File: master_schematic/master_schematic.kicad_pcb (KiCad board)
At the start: 4 copper layers, 157.5 x 111.9 mm, 82 parts, among them J1 Conn_01x02_Shielded, J10 0430450400, J11 1723103102, J12 1723103102, J13 1723103102, J14 1723103102, J15 1723103102, J16 1723103102, J17 1723103102, J18 1723103102, J19 1723103102, J2 0430450400, J20 1723103102, J3 0430450400, J4 0430450400, J5 0430450400, J6 0430450400, J7 0430450400, J8 0430450400, J9 0430450400, Q1 CWDM3011N TR13 PBFREE, Q10 CWDM3011N TR13 PBFREE, Q2 CWDM3011N TR13 PBFREE, Q3 CWDM3011N TR13 PBFREE, Q4 CWDM3011N TR13 PBFREE, Q5 CWDM3011N TR13 PBFREE, Q6 CWDM3011N TR13 PBFREE, Q7 CWDM3011N TR13 PBFREE, Q8 CWDM3011N TR13 PBFREE, Q9 CWDM3011N TR13 PBFREE, U1 RFM95, U10 HX711, U11 HX711, U2 teensy_4.1, U4 MCP9600_Module, U5 MCP9600_Module, U6 MCP9600_Module, U7 MCP9600_Module, U8 MCP9600_Module, U9 HX711

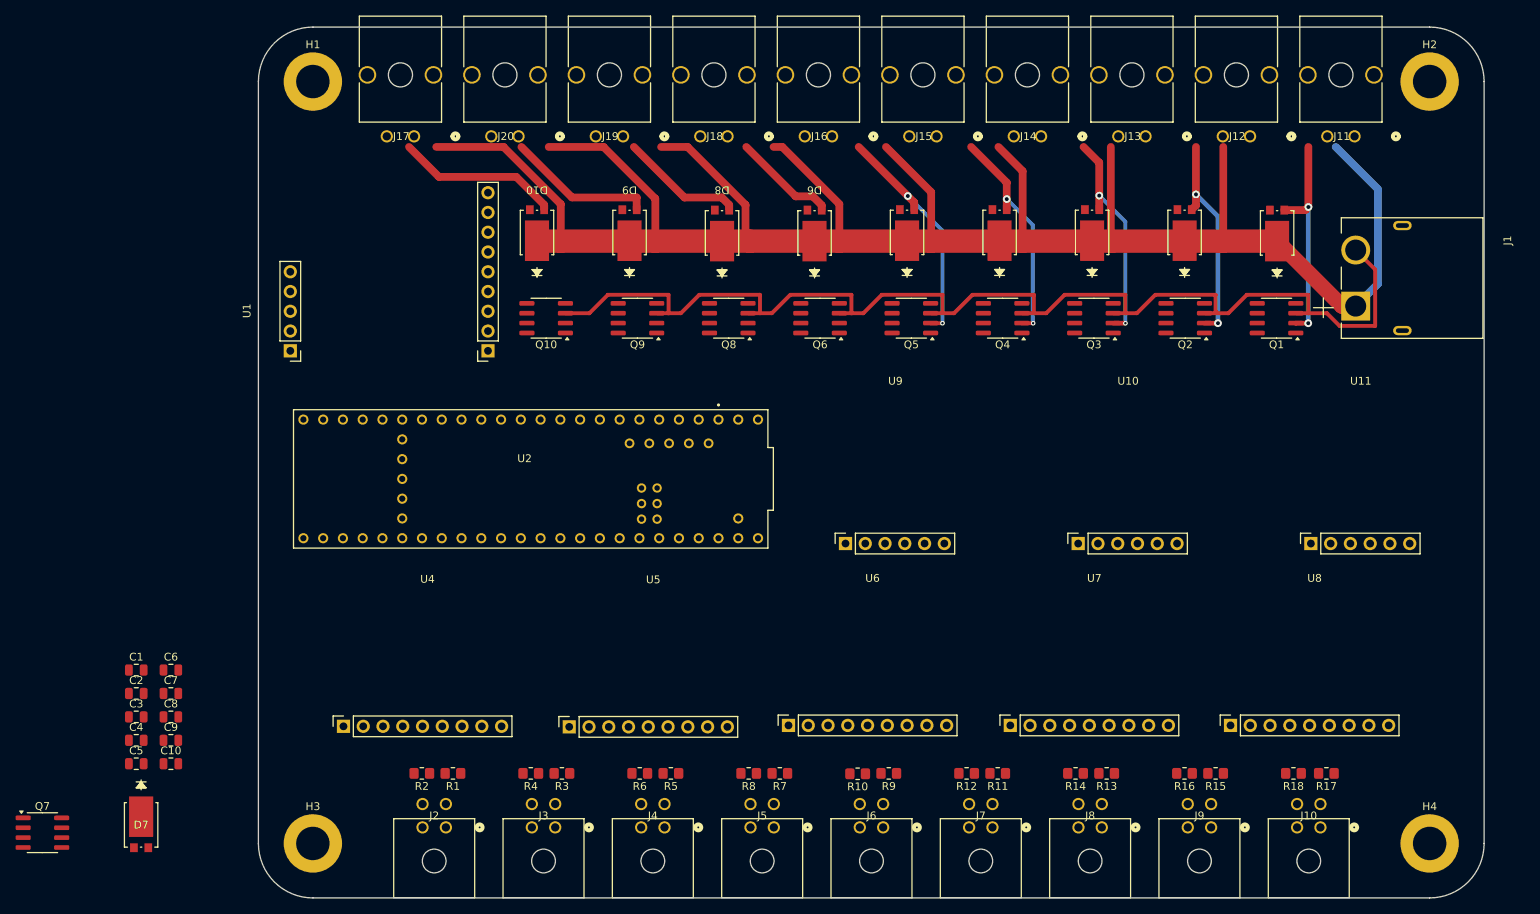
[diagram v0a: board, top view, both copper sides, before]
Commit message: fixed errors, redesigned PCB layout
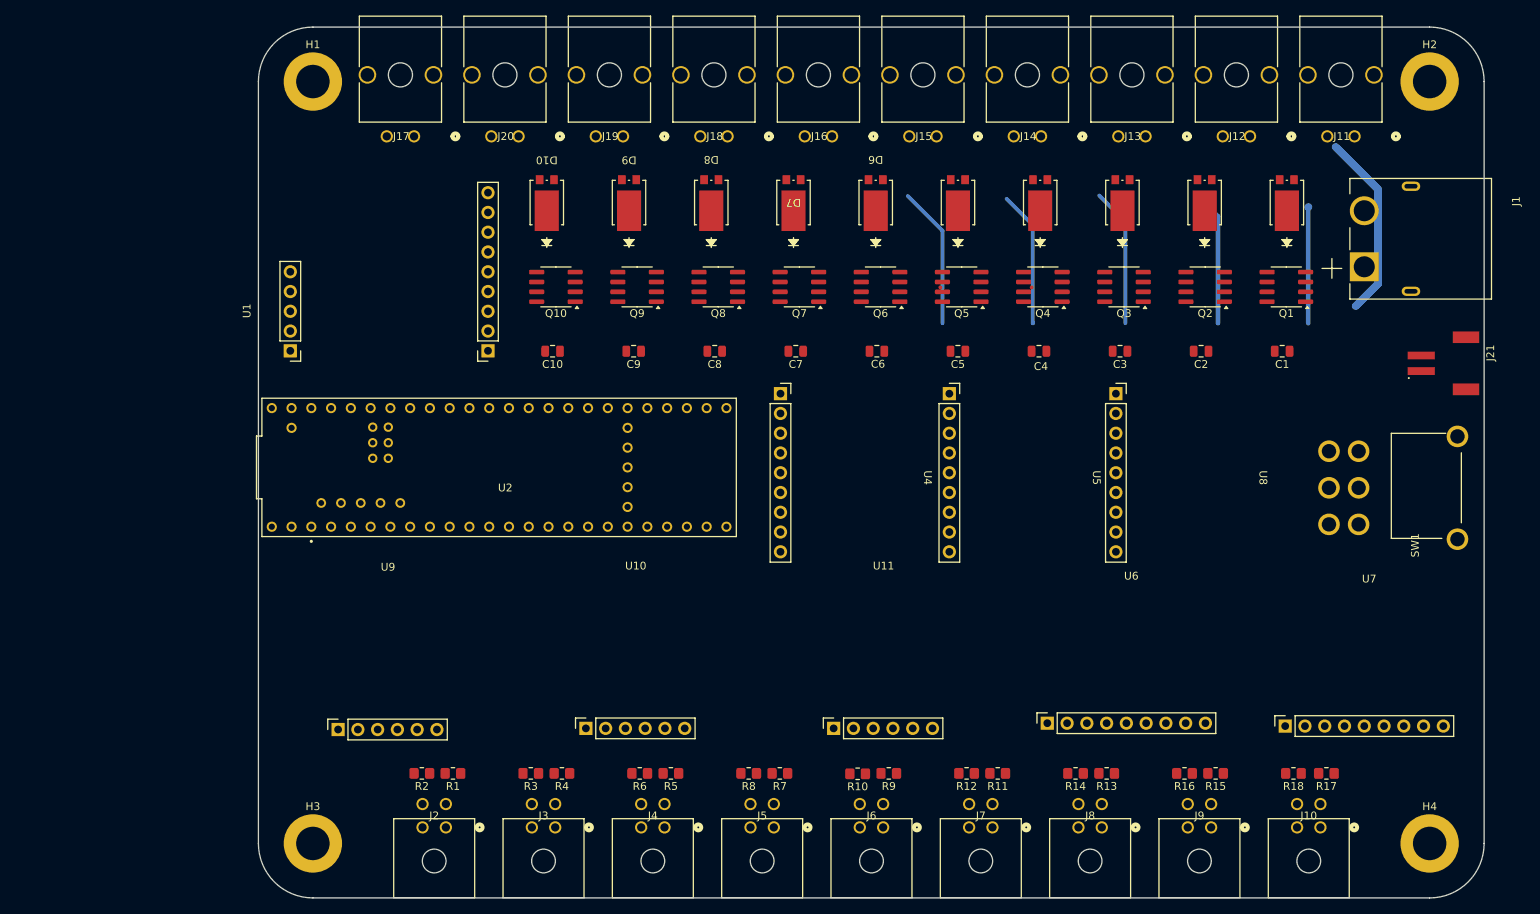
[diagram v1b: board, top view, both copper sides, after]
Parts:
- added J21: 5V Female, hb_footprint_lib:JST_S2B-PH-SM4-TB, F.Cu at (174.4, 64.2)
- added SW1: SW_SPST, hb_footprint_lib:SW_1201M2S3AQE2, F.Cu at (179.1, 80.2)
- J1: value Conn_01x02_Shielded -> 12V Female
- R3: renamed from R4; value 2.7K -> 1K
- R4: renamed from R3; value 1K -> 2.7K
- moved C1 152.8 mm to (156.6, 62.6), turned to 180 degrees
- moved C2 143.7 mm to (146.1, 62.6), turned to 180 degrees
- moved C3 134.9 mm to (135.7, 62.6), turned to 180 degrees
- moved C4 126.3 mm to (125.3, 62.6), turned to 180 degrees
- moved Q7 119.9 mm to (94.5, 54.4), turned to 180 degrees
- moved C5 118.1 mm to (114.9, 62.6), turned to 180 degrees
- moved D7 115.9 mm to (93.8, 43.5), turned to 180 degrees
- moved C6 99.5 mm to (104.5, 62.6), turned to 180 degrees
- moved C7 91.5 mm to (94.1, 62.6), turned to 180 degrees
- moved C8 84.2 mm to (83.6, 62.6), turned to 180 degrees
- moved C9 77.7 mm to (73.2, 62.6), turned to 180 degrees
- moved C10 72.2 mm to (62.8, 62.6), turned to 180 degrees
- moved U9 69.4 mm to (41.6, 90.9)
- moved U10 67.6 mm to (73.5, 90.7)
- moved U11 65.8 mm to (105.3, 90.7)
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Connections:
- R3 pad 1: /PT1_N -> /pressure_transducers/PT1_N_RAW
- R3 pad 2: GND -> /PT1_N
- R4 pad 1: /pressure_transducers/PT1_N_RAW -> /PT1_N
- R4 pad 2: /PT1_N -> GND
- U4 pad 9: (no net) -> unconnected-(U4-ADDR-Pad9)
- U5 pad 9: (no net) -> unconnected-(U5-ADDR-Pad9)
- U6 pad 9: (no net) -> unconnected-(U6-ADDR-Pad9)
- U7 pad 9: (no net) -> unconnected-(U7-ADDR-Pad9)
- U8 pad 9: (no net) -> unconnected-(U8-ADDR-Pad9)
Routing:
- net +12V: track 265.5 -> 23.9 mm
- net GND: track 154.7 -> 17.4 mm
- net Net-(D4-A): track 28.8 -> 0.01 mm, vias 2 -> 0
- net Net-(D3-A): track 28.2 -> 0.00 mm, vias 2 -> 0
- net Net-(D2-A): track 27.7 -> 0.00 mm, vias 2 -> 0
- net Net-(D10-A): track 21.1 -> 0.00 mm
- net Net-(D9-A): track 19.1 -> 0.00 mm
- net unconnected-(U8-A2-Pad6): track 0.00 -> 17.8 mm
- net +3V3: track 0.00 -> 17.7 mm
- net Net-(D8-A): track 16.0 -> 0.00 mm
- net Net-(D6-A): track 13.4 -> 0.00 mm
- net Net-(D1-A): track 27.5 -> 14.9 mm, vias 2 -> 0
- net Net-(D5-A): track 30.7 -> 18.2 mm, vias 2 -> 0

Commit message: redid power layer
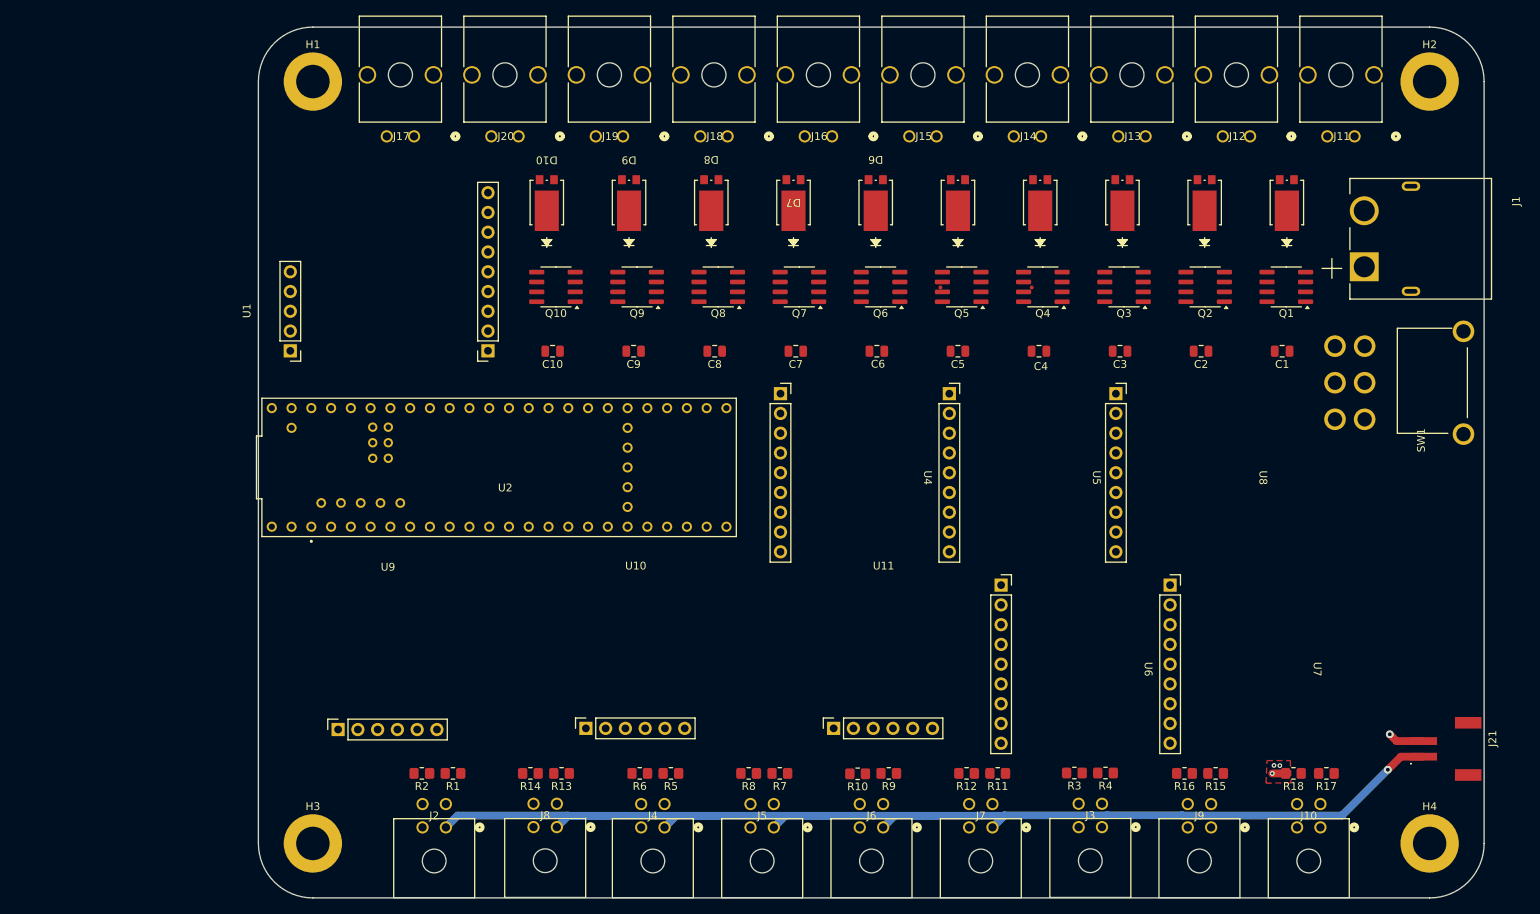
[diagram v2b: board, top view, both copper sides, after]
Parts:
- moved J3 70.3 mm to (133.4, 123.8)
- moved R13 70.0 mm to (64.0, 116.9)
- moved R14 70.0 mm to (60.0, 116.9)
- moved J8 70.0 mm to (63.4, 123.8)
- moved R3 69.9 mm to (129.8, 116.8)
- moved R4 69.9 mm to (133.8, 116.8)
- moved J21 49.6 mm to (174.7, 113.8)
- moved SW1 13.5 mm to (179.8, 66.7)
- moved U7 13.2 mm to (160.6, 103.5), turned to -90 degrees
- moved U6 11.6 mm to (138.8, 103.5), turned to -90 degrees
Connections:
- U1 pad 1: +5V -> +3V3
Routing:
- net +5V: track 0.00 -> 140.0 mm, vias 0 -> 1
- net +12V: track 23.9 -> 0.00 mm
- net Net-(D5-A): track 18.2 -> 0.01 mm
- net unconnected-(U8-A2-Pad6): track 17.8 -> 0.00 mm
- net +3V3: track 17.7 -> 0.00 mm
- net Net-(D1-A): track 14.9 -> 0.00 mm
- net GND: track 17.4 -> 6.41 mm, vias 0 -> 4
- added copper zone on In2.Cu, net +12V
- added copper zone on In2.Cu, net +3V3
- added copper zone on F.Cu, net GND
- removed copper zone on In2.Cu, net +5V
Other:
- board text added: "PWR"
- board text removed: "+5V"

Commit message: routed some annoying ass traces
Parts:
- moved R4 4.13 mm to (129.7, 116.9)
- moved R3 3.88 mm to (133.7, 116.8)
- moved U5 3.55 mm to (135.7, 78.6)
- moved U4 3.55 mm to (114.0, 78.6)
- moved U8 3.55 mm to (157.1, 78.6)
- moved U2 1.38 mm to (57.3, 77.6)
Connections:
- U2 pad VIN: (no net) -> +5V
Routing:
- net /PT5_I: track 0.00 -> 155.9 mm
- net /PT4_I: track 0.00 -> 147.5 mm
- net /PV1_N: track 0.00 -> 141.0 mm, vias 0 -> 1
- net /PT1_N: track 0.00 -> 140.3 mm
- net /PT2_I: track 0.00 -> 127.0 mm
- net /PV1_P: track 0.00 -> 111.0 mm, vias 0 -> 1
- net +5V: track 140.0 -> 208.0 mm
- net /LC3_RATE: track 0.00 -> 63.4 mm
- net /MBV1-I-2: track 0.00 -> 62.2 mm, vias 0 -> 1
- net /LC3_DATA: track 0.00 -> 58.9 mm
- net /PT1_T: track 0.00 -> 55.2 mm
- net /BV1-P: track 0.00 -> 54.5 mm, vias 0 -> 1
- net /LC1_DATA: track 0.00 -> 52.9 mm
- net /LC2_RATE: track 0.00 -> 51.6 mm
- net /LC2_DATA: track 0.00 -> 47.8 mm
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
